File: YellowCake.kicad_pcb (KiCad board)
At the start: 2 copper layers, 95.9 x 90.2 mm, 4 parts

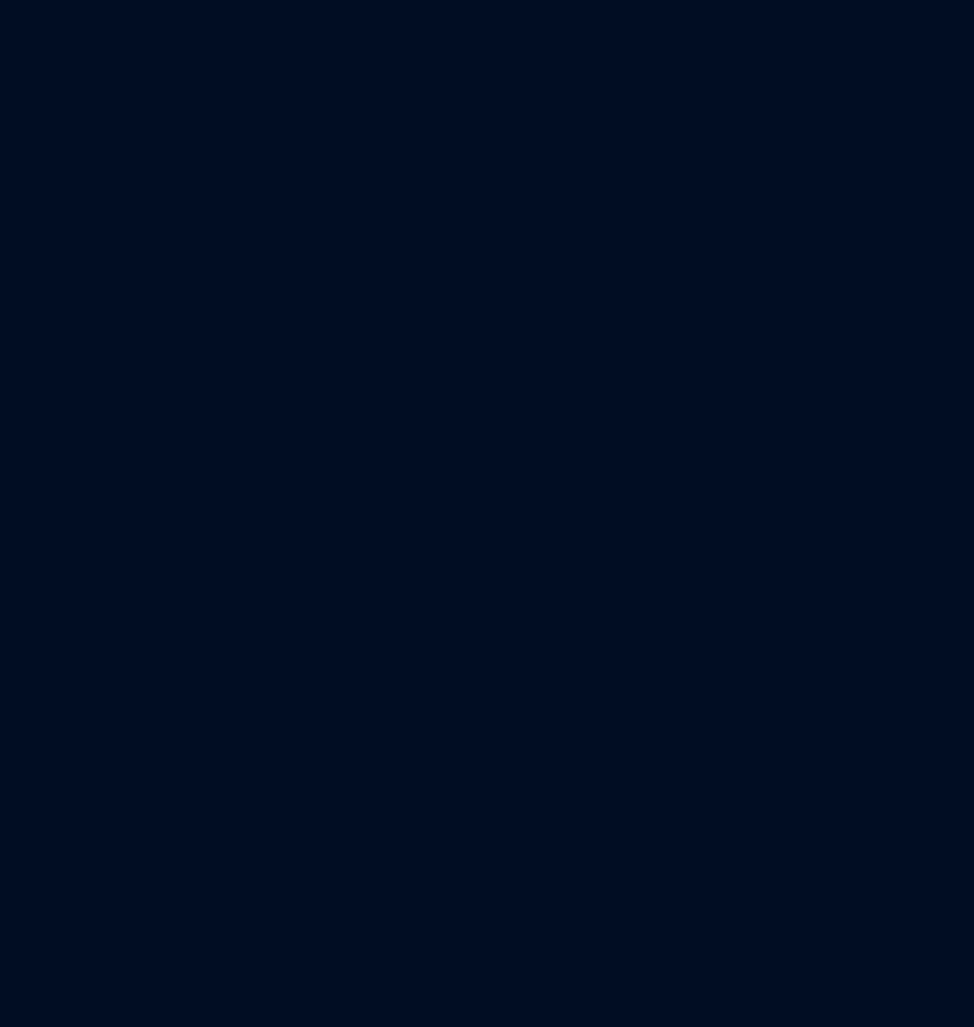
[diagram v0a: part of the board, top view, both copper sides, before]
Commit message: started power supply and DAC circuitry
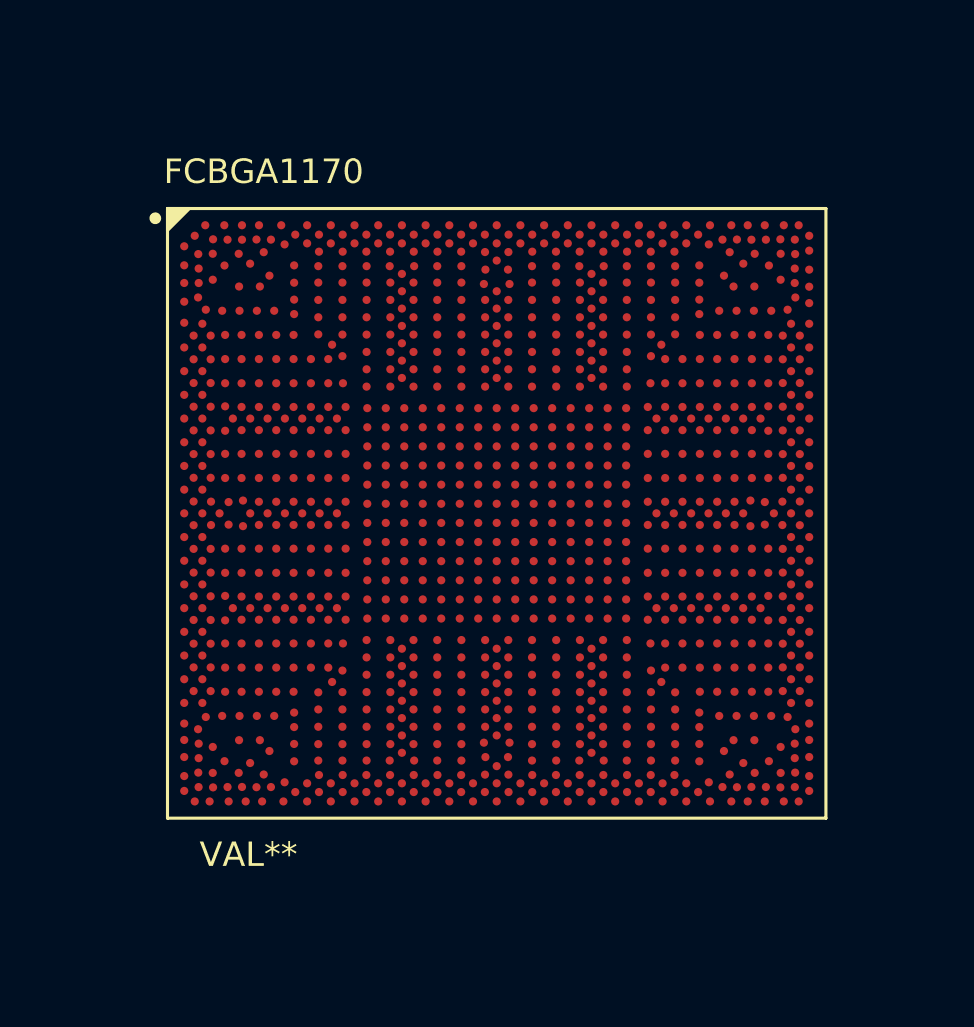
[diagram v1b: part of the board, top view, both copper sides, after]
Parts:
- added FCBGA1170: VAL**, Atom:FCBGA11702, F.Cu at (151.0, 83.0)

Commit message: finishing schematic
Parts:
- added C1, C11, C12, C14, C18, C21, C30, C34, C52, C53, C54, C55, C56, C57, C58, C61, C62, C66, C69, C71, C78, C79, C80, C81, C82, C83, C84, C85, C86, C9, C94, C95: 0.1uF, Capacitor_SMD:C_0603_1608Metric, F.Cu at (148.9, 138.3)
- added C10, C7: 10uF, Capacitor_Tantalum_SMD:CP_EIA-2012-15_AVX-P, F.Cu at (148.9, 138.3)
- added C100, C2, C3, C6, C96, C98: 1uF, Capacitor_SMD:C_0603_1608Metric, F.Cu at (148.9, 138.3)
- added C101: 4700PF, Capacitor_SMD:C_0603_1608Metric, F.Cu at (148.9, 138.3)
- added C102, C103, C13, C15, C76, C8, C89, C91, C97, C99: 10uF, Capacitor_SMD:C_0603_1608Metric, F.Cu at (148.9, 138.3)
- added C16, C17, C31, C33: 1000pF, Capacitor_SMD:C_0603_1608Metric, F.Cu at (148.9, 138.3)
- added C19, C22: 330pF, Capacitor_SMD:C_0603_1608Metric, F.Cu at (148.9, 138.3)
- added C20, C23: 0.01uF, Capacitor_SMD:C_0603_1608Metric, F.Cu at (148.9, 138.3)
- added C24, C28: 560pF, Capacitor_SMD:C_0603_1608Metric, F.Cu at (148.9, 138.3)
- added C25: 470pF, Capacitor_SMD:C_0603_1608Metric, F.Cu at (148.9, 138.3)
- added C26: 68pF, Capacitor_SMD:C_0603_1608Metric, F.Cu at (148.9, 138.3)
- added C27: 220pF, Capacitor_SMD:C_0603_1608Metric, F.Cu at (148.9, 138.3)
- added C29: 33pF, Capacitor_SMD:C_0603_1608Metric, F.Cu at (148.9, 138.3)
- added C32, C35, C37, C72, C77: 1.0uF, Capacitor_SMD:C_0603_1608Metric, F.Cu at (148.9, 138.3)
- added C36, C38, C39, C75: 0.22uF, Capacitor_SMD:C_0603_1608Metric, F.Cu at (148.9, 138.3)
- added C4, C5: 2.2uF, Capacitor_SMD:C_0603_1608Metric, F.Cu at (148.9, 138.3)
- added C40, C41: 2200pF, Capacitor_SMD:C_0603_1608Metric, F.Cu at (148.9, 138.3)
- added C42, C43: 0.047uF, Capacitor_SMD:C_0603_1608Metric, F.Cu at (148.9, 138.3)
- added C44, C45, C46, C47, C48, C49: 0.033uF, Capacitor_SMD:C_0603_1608Metric, F.Cu at (148.9, 138.3)
- added C59, C60, C67, C68, C70, C73, C74, C87, C88, C90, C92, C93: 22uF, Capacitor_SMD:C_0603_1608Metric, F.Cu at (148.9, 138.3)
- added C65: 8200pF, Resistor_SMD:R_0603_1608Metric, F.Cu at (148.9, 138.3)
- added D1, D4: BAT54A, Package_TO_SOT_SMD:SOT-23, F.Cu at (148.9, 138.3)
- added D2, D3: BAV99S, Package_TO_SOT_SMD:SOT-363_SC-70-6, F.Cu at (148.9, 138.3)
- added L1, L7, L8: 220Ohm, Inductor_SMD:L_0603_1608Metric, F.Cu at (148.9, 138.3)
- added L10, L4: 0Ohm, Inductor_SMD:L_0603_1608Metric, F.Cu at (148.9, 138.3)
- added L15: PIND-2.2U-8A, Inductor_SMD:L_0603_1608Metric, F.Cu at (148.9, 138.3)
- added Q1, Q2, Q4, Q5, Q6: 2N7002K, Package_TO_SOT_SMD:SOT-23, F.Cu at (148.9, 138.3)
- added Q3: MMBT3904, Package_TO_SOT_SMD:SOT-23, F.Cu at (148.9, 138.3)
- added R1, R2: 2.2kOhm, Resistor_SMD:R_0603_1608Metric, F.Cu at (148.9, 138.3)
- added R10, R32, R34, R36, R38, R39, R42, R43, R7, R8, R9: 0Ohm, Resistor_SMD:R_0603_1608Metric, F.Cu at (148.9, 138.3)
- added R100, R76, R77, R78, R79, R80, R81, R85, R87, R95, R97: 100KOhm, Resistor_SMD:R_0603_1608Metric, F.Cu at (148.9, 138.3)
- added R101: 200KOhm, Resistor_SMD:R_0603_1608Metric, F.Cu at (148.9, 138.3)
- added R11, R12, R14, R15: 10Ohm, Resistor_SMD:R_0603_1608Metric, F.Cu at (148.9, 138.3)
- added R13: 2.7KOhm, Resistor_SMD:R_0603_1608Metric, F.Cu at (148.9, 138.3)
- added R16: 2.32KOhm, Resistor_SMD:R_0603_1608Metric, F.Cu at (148.9, 138.3)
- added R17, R19: 200Ohm, Resistor_SMD:R_0603_1608Metric, F.Cu at (148.9, 138.3)
- added R18: 2.43KOhm, Resistor_SMD:R_0603_1608Metric, F.Cu at (148.9, 138.3)
- added R20, R23, R27: 80.6KOhm, Resistor_SMD:R_0603_1608Metric, F.Cu at (148.9, 138.3)
- added R21: 2.21KOhm, Resistor_SMD:R_0603_1608Metric, F.Cu at (148.9, 138.3)
- added R22, R24, R25: 69.8Ohm, Resistor_SMD:R_0603_1608Metric, F.Cu at (148.9, 138.3)
- added R26: 169KOhm, Resistor_SMD:R_0603_1608Metric, F.Cu at (148.9, 138.3)
- added R28, R30: 1.91KOhm, Resistor_SMD:R_0603_1608Metric, F.Cu at (148.9, 138.3)
- added R29, R31: 6.98KOhm, Resistor_SMD:R_0603_1608Metric, F.Cu at (148.9, 138.3)
- added R3, R4, R70, R71, R72, R73, R74, R75, R88: 33Ohm, Resistor_SMD:R_0603_1608Metric, F.Cu at (148.9, 138.3)
- added R33: 16.9Ohm, Resistor_SMD:R_0603_1608Metric, F.Cu at (148.9, 138.3)
- added R35: 20Ohm, Resistor_SMD:R_0603_1608Metric, F.Cu at (148.9, 138.3)
- added R37, R90, R91, R94: 1KOhm, Resistor_SMD:R_0603_1608Metric, F.Cu at (148.9, 138.3)
- added R40: 1Ohm, Resistor_SMD:R_0603_1608Metric, F.Cu at (148.9, 138.3)
- added R41, R48: 18.7KOhm, Resistor_SMD:R_0603_1608Metric, F.Cu at (148.9, 138.3)
- added R44, R47: 3.83KOhm, Resistor_SMD:R_0603_1608Metric, F.Cu at (148.9, 138.3)
- added R45, R46: NTC-470KOhm, Resistor_SMD:R_0603_1608Metric, F.Cu at (148.9, 138.3)
- added R49, R50: 649Ohm, Resistor_SMD:R_0603_1608Metric, F.Cu at (148.9, 138.3)
- added R5: 37.4KOhm, Resistor_SMD:R_0603_1608Metric, F.Cu at (148.9, 138.3)
- added R51: 2.67KOhm, Resistor_SMD:R_0603_1608Metric, F.Cu at (148.9, 138.3)
- added R52, R57: 2.61KOhm, Resistor_SMD:R_0603_1608Metric, F.Cu at (148.9, 138.3)
- added R53, R54: 11KOhm, Resistor_SMD:R_0603_1608Metric, F.Cu at (148.9, 138.3)
- added R55, R58: NTC-10KOhm, Resistor_SMD:R_0603_1608Metric, F.Cu at (148.9, 138.3)
- added R56: 2.55KOhm, Resistor_SMD:R_0603_1608Metric, F.Cu at (148.9, 138.3)
- added R6: 12.1KOhm, Resistor_SMD:R_0603_1608Metric, F.Cu at (148.9, 138.3)
- added R82, R84: 499KOhm, Resistor_SMD:R_0603_1608Metric, F.Cu at (148.9, 138.3)
- added R83: 2.2Ohms, Resistor_SMD:R_0603_1608Metric, F.Cu at (148.9, 138.3)
- added R86: 4.7Ohm, Resistor_SMD:R_0603_1608Metric, F.Cu at (148.9, 138.3)
- added R89: 2.2KOhm, Resistor_SMD:R_0603_1608Metric, F.Cu at (148.9, 138.3)
- added R92, R93: 10KOhm, Resistor_SMD:R_0603_1608Metric, F.Cu at (148.9, 138.3)
- added R99: 33KOhm, Resistor_SMD:R_0603_1608Metric, F.Cu at (148.9, 138.3)
- added U2: ISL95837HRZ-T, Package_DFN_QFN:QFN-40-1EP_6x6mm_P0.5mm_EP4.6x4.6mm, F.Cu at (148.9, 138.3)
- added U6: TPD4EUSB30, Package_SON:USON-10_2.5x1.0mm_P0.5mm, F.Cu at (148.9, 138.3)
- added U8: TPD6E001RSER, TPD6E001RSER:TPD6E001RSER, F.Cu at (148.9, 138.3)

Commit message: finished fixes
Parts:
- removed C1, C11, C12, C14, C18, C21, C30, C34, C52, C53, C54, C55, C56, C57, C58, C61, C62, C66, C69, C71, C78, C79, C80, C81, C82, C83, C84, C85, C86, C9, C94, C95: 0.1uF, Capacitor_SMD:C_0603_1608Metric
- removed C10, C7: 10uF, Capacitor_Tantalum_SMD:CP_EIA-2012-15_AVX-P
- removed C100, C2, C3, C6, C96, C98: 1uF, Capacitor_SMD:C_0603_1608Metric
- removed C101: 4700PF, Capacitor_SMD:C_0603_1608Metric
- removed C102, C103, C13, C15, C76, C8, C89, C91, C97, C99: 10uF, Capacitor_SMD:C_0603_1608Metric
- removed C16, C17, C31, C33: 1000pF, Capacitor_SMD:C_0603_1608Metric
- removed C19, C22: 330pF, Capacitor_SMD:C_0603_1608Metric
- removed C20, C23: 0.01uF, Capacitor_SMD:C_0603_1608Metric
- removed C24, C28: 560pF, Capacitor_SMD:C_0603_1608Metric
- removed C25: 470pF, Capacitor_SMD:C_0603_1608Metric
- removed C26: 68pF, Capacitor_SMD:C_0603_1608Metric
- removed C27: 220pF, Capacitor_SMD:C_0603_1608Metric
- removed C29: 33pF, Capacitor_SMD:C_0603_1608Metric
- removed C32, C35, C37, C72, C77: 1.0uF, Capacitor_SMD:C_0603_1608Metric
- removed C36, C38, C39, C75: 0.22uF, Capacitor_SMD:C_0603_1608Metric
- removed C4, C5: 2.2uF, Capacitor_SMD:C_0603_1608Metric
- removed C40, C41: 2200pF, Capacitor_SMD:C_0603_1608Metric
- removed C42, C43: 0.047uF, Capacitor_SMD:C_0603_1608Metric
- removed C44, C45, C46, C47, C48, C49: 0.033uF, Capacitor_SMD:C_0603_1608Metric
- removed C59, C60, C67, C68, C70, C73, C74, C87, C88, C90, C92, C93: 22uF, Capacitor_SMD:C_0603_1608Metric
- removed C65: 8200pF, Resistor_SMD:R_0603_1608Metric
- removed D1, D4: BAT54A, Package_TO_SOT_SMD:SOT-23
- removed D2, D3: BAV99S, Package_TO_SOT_SMD:SOT-363_SC-70-6
- removed L1, L7, L8: 220Ohm, Inductor_SMD:L_0603_1608Metric
- removed L10, L4: 0Ohm, Inductor_SMD:L_0603_1608Metric
- removed L15: PIND-2.2U-8A, Inductor_SMD:L_0603_1608Metric
- removed Q1, Q2, Q4, Q5, Q6: 2N7002K, Package_TO_SOT_SMD:SOT-23
- removed Q3: MMBT3904, Package_TO_SOT_SMD:SOT-23
- removed R1, R2: 2.2kOhm, Resistor_SMD:R_0603_1608Metric
- removed R10, R32, R34, R36, R38, R39, R42, R43, R7, R8, R9: 0Ohm, Resistor_SMD:R_0603_1608Metric
- removed R100, R76, R77, R78, R79, R80, R81, R85, R87, R95, R97: 100KOhm, Resistor_SMD:R_0603_1608Metric
- removed R101: 200KOhm, Resistor_SMD:R_0603_1608Metric
- removed R11, R12, R14, R15: 10Ohm, Resistor_SMD:R_0603_1608Metric
- removed R13: 2.7KOhm, Resistor_SMD:R_0603_1608Metric
- removed R16: 2.32KOhm, Resistor_SMD:R_0603_1608Metric
- removed R17, R19: 200Ohm, Resistor_SMD:R_0603_1608Metric
- removed R18: 2.43KOhm, Resistor_SMD:R_0603_1608Metric
- removed R20, R23, R27: 80.6KOhm, Resistor_SMD:R_0603_1608Metric
- removed R21: 2.21KOhm, Resistor_SMD:R_0603_1608Metric
- removed R22, R24, R25: 69.8Ohm, Resistor_SMD:R_0603_1608Metric
- removed R26: 169KOhm, Resistor_SMD:R_0603_1608Metric
- removed R28, R30: 1.91KOhm, Resistor_SMD:R_0603_1608Metric
- removed R29, R31: 6.98KOhm, Resistor_SMD:R_0603_1608Metric
- removed R3, R4, R70, R71, R72, R73, R74, R75, R88: 33Ohm, Resistor_SMD:R_0603_1608Metric
- removed R33: 16.9Ohm, Resistor_SMD:R_0603_1608Metric
- removed R35: 20Ohm, Resistor_SMD:R_0603_1608Metric
- removed R37, R90, R91, R94: 1KOhm, Resistor_SMD:R_0603_1608Metric
- removed R40: 1Ohm, Resistor_SMD:R_0603_1608Metric
- removed R41, R48: 18.7KOhm, Resistor_SMD:R_0603_1608Metric
- removed R44, R47: 3.83KOhm, Resistor_SMD:R_0603_1608Metric
- removed R45, R46: NTC-470KOhm, Resistor_SMD:R_0603_1608Metric
- removed R49, R50: 649Ohm, Resistor_SMD:R_0603_1608Metric
- removed R5: 37.4KOhm, Resistor_SMD:R_0603_1608Metric
- removed R51: 2.67KOhm, Resistor_SMD:R_0603_1608Metric
- removed R52, R57: 2.61KOhm, Resistor_SMD:R_0603_1608Metric
- removed R53, R54: 11KOhm, Resistor_SMD:R_0603_1608Metric
- removed R55, R58: NTC-10KOhm, Resistor_SMD:R_0603_1608Metric
- removed R56: 2.55KOhm, Resistor_SMD:R_0603_1608Metric
- removed R6: 12.1KOhm, Resistor_SMD:R_0603_1608Metric
- removed R82, R84: 499KOhm, Resistor_SMD:R_0603_1608Metric
- removed R83: 2.2Ohms, Resistor_SMD:R_0603_1608Metric
- removed R86: 4.7Ohm, Resistor_SMD:R_0603_1608Metric
- removed R89: 2.2KOhm, Resistor_SMD:R_0603_1608Metric
- removed R92, R93: 10KOhm, Resistor_SMD:R_0603_1608Metric
- removed R99: 33KOhm, Resistor_SMD:R_0603_1608Metric
- removed U2: ISL95837HRZ-T, Package_DFN_QFN:QFN-40-1EP_6x6mm_P0.5mm_EP4.6x4.6mm
- removed U6: TPD4EUSB30, Package_SON:USON-10_2.5x1.0mm_P0.5mm
- removed U8: TPD6E001RSER, TPD6E001RSER:TPD6E001RSER
- added TRANS_FDMD8530: VAL**, FDMS7602S:TRANS_FDMD8530, F.Cu at (174.6, 98.2)

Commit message: Finished all except RAM and CPU
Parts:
- removed REF** (x4): MountingHole_3.2mm_M3_Pad, MountingHole:MountingHole_3.2mm_M3_Pad
- removed TRANS_FDMD8530: VAL**, FDMS7602S:TRANS_FDMD8530
- added C1: 0.1uF, Capacitor_SMD:C_0603_1608Metric, F.Cu at (322.0, 119.4)
- added C10: 10uF, Capacitor_Tantalum_SMD:CP_EIA-2012-15_AVX-P, F.Cu at (318.5, 109.2)
- added C100: 1uF, Capacitor_SMD:C_0603_1608Metric, F.Cu at (152.4, 196.3)
- added C101: 4700PF, Capacitor_SMD:C_0603_1608Metric, F.Cu at (172.9, 180.9)
- added C102: 10uF, Capacitor_SMD:C_0603_1608Metric, F.Cu at (173.4, 175.9)
- added C103: 10uF, Capacitor_SMD:C_0603_1608Metric, F.Cu at (164.0, 188.9)
- added C104: 2.2uF, Capacitor_SMD:C_0603_1608Metric, F.Cu at (168.4, 183.0)
- added C105: 2.2uF, Capacitor_SMD:C_0603_1608Metric, F.Cu at (172.9, 178.4)
- added C106: 22pF, Capacitor_SMD:C_0603_1608Metric, F.Cu at (153.7, 198.9)
- added C107: 22pF, Capacitor_SMD:C_0603_1608Metric, F.Cu at (156.4, 195.6)
- added C108: 22pF, Capacitor_SMD:C_0603_1608Metric, F.Cu at (177.4, 173.4)
- added C109: 27pF, Capacitor_SMD:C_0603_1608Metric, F.Cu at (156.4, 193.1)
- added C11: 0.1uF, Capacitor_SMD:C_0603_1608Metric, F.Cu at (322.2, 114.3)
- added C110: 10uF, Capacitor_SMD:C_0603_1608Metric, F.Cu at (149.7, 198.9)
- added C111: 0.1uF, Capacitor_SMD:C_0603_1608Metric, F.Cu at (168.2, 186.3)
- added C112: 10uF, Capacitor_SMD:C_0603_1608Metric, F.Cu at (137.7, 200.1)
- added C113: 0.1uF, Capacitor_SMD:C_0603_1608Metric, F.Cu at (168.9, 180.5)
- added C114: 10uF, Capacitor_SMD:C_0603_1608Metric, F.Cu at (160.0, 189.9)
- added C115: 22pF, Capacitor_SMD:C_0603_1608Metric, F.Cu at (164.2, 186.3)
- added C116: 10uF, Capacitor_SMD:C_0603_1608Metric, F.Cu at (160.0, 187.4)
- added C117: 1.0uF, Capacitor_SMD:C_0603_1608Metric, F.Cu at (145.7, 199.8)
- added C118: 10uF, Capacitor_SMD:C_0603_1608Metric, F.Cu at (152.4, 193.8)
- added C119: 1uF, Capacitor_SMD:C_0603_1608Metric, F.Cu at (180.2, 185.9)
- added C12: 0.1uF, Capacitor_SMD:C_0603_1608Metric, F.Cu at (314.0, 117.8)
- added C120: 0.1uF, Capacitor_SMD:C_0603_1608Metric, F.Cu at (336.4, 183.8)
- added C121: 0.1uF, Capacitor_SMD:C_0603_1608Metric, F.Cu at (332.5, 188.8)
- added C122: 22uF, Capacitor_SMD:C_0603_1608Metric, F.Cu at (340.4, 180.7)
- added C123: 22uF, Capacitor_SMD:C_0603_1608Metric, F.Cu at (336.5, 186.3)
- added C124: 22uF, Capacitor_SMD:C_0603_1608Metric, F.Cu at (326.2, 176.5)
- added C125: 22uF, Capacitor_SMD:C_0603_1608Metric, F.Cu at (328.5, 186.6)
- added C126: 2200pF, Capacitor_SMD:C_0603_1608Metric, F.Cu at (316.4, 183.1)
- added C127: 2200pF, Capacitor_SMD:C_0603_1608Metric, F.Cu at (316.4, 185.6)
- added C128: 22uF, Capacitor_SMD:C_0603_1608Metric, F.Cu at (312.5, 188.9)
- added C129: 22uF, Capacitor_SMD:C_0603_1608Metric, F.Cu at (327.5, 173.7)
- added C13: 10uF, Capacitor_SMD:C_0603_1608Metric, F.Cu at (318.0, 120.3)
- added C130: 22uF, Capacitor_SMD:C_0603_1608Metric, F.Cu at (332.3, 170.7)
- added C131: 22uF, Capacitor_SMD:C_0603_1608Metric, F.Cu at (320.4, 183.1)
- added C132: 22uF, Capacitor_SMD:C_0603_1608Metric, F.Cu at (326.2, 179.0)
- added C133: 22uF, Capacitor_SMD:C_0603_1608Metric, F.Cu at (331.5, 173.7)
- added C134: 330uF, Capacitor_Tantalum_SMD:CP_EIA-7343-20_Kemet-V, F.Cu at (310.7, 178.2)
- added C135: 330uF, Capacitor_Tantalum_SMD:CP_EIA-7343-20_Kemet-V, F.Cu at (320.5, 172.3)
- added C136: 330uF, Capacitor_Tantalum_SMD:CP_EIA-7343-20_Kemet-V, F.Cu at (310.7, 172.3)
- added C137: 22uF, Capacitor_SMD:C_0603_1608Metric, F.Cu at (324.4, 183.1)
- added C138: 22uF, Capacitor_SMD:C_0603_1608Metric, F.Cu at (316.5, 190.6)
- added C139: 22uF, Capacitor_SMD:C_0603_1608Metric, F.Cu at (330.3, 178.7)
- added C14: 0.1uF, Capacitor_SMD:C_0603_1608Metric, F.Cu at (326.3, 111.5)
- added C140: 22uF, Capacitor_SMD:C_0603_1608Metric, F.Cu at (320.5, 188.1)
- added C141: 22uF, Capacitor_SMD:C_0603_1608Metric, F.Cu at (335.5, 173.2)
- added C142: 22uF, Capacitor_SMD:C_0603_1608Metric, F.Cu at (334.3, 176.2)
- added C143: 22uF, Capacitor_SMD:C_0603_1608Metric, F.Cu at (342.3, 178.2)
- added C144: 22uF, Capacitor_SMD:C_0603_1608Metric, F.Cu at (324.4, 185.6)
- added C145: 22uF, Capacitor_SMD:C_0603_1608Metric, F.Cu at (340.4, 183.2)
- added C146: 22uF, Capacitor_SMD:C_0603_1608Metric, F.Cu at (334.3, 178.7)
- added C147: 22uF, Capacitor_SMD:C_0603_1608Metric, F.Cu at (320.5, 190.6)
- added C148: 22uF, Capacitor_SMD:C_0603_1608Metric, F.Cu at (328.4, 181.5)
- added C149: 0.1uF, Capacitor_SMD:C_0603_1608Metric, F.Cu at (337.2, 136.0)
- added C15: 10uF, Capacitor_SMD:C_0603_1608Metric, F.Cu at (322.0, 116.9)
- added C150: 22uF, Capacitor_SMD:C_0603_1608Metric, F.Cu at (332.2, 141.3)
- added C151: 0.1uF, Capacitor_SMD:C_0603_1608Metric, F.Cu at (340.2, 146.1)
- added C152: 10uF, Capacitor_SMD:C_0603_1608Metric, F.Cu at (340.2, 143.6)
- added C153: 22uF, Capacitor_SMD:C_0603_1608Metric, F.Cu at (345.2, 138.6)
- added C154: 150pF, Capacitor_SMD:C_0603_1608Metric, F.Cu at (335.8, 148.8)
- added C155: 150pF, Capacitor_SMD:C_0603_1608Metric, F.Cu at (336.2, 146.1)
- added C156: 0.1uF, Capacitor_SMD:C_0603_1608Metric, F.Cu at (345.2, 136.0)
- added C157: 0.1uF, Capacitor_SMD:C_0603_1608Metric, F.Cu at (340.2, 141.1)
- added C158: 0.1uF, Capacitor_SMD:C_0603_1608Metric, F.Cu at (327.8, 148.9)
- added C159: 0.1uF, Capacitor_SMD:C_0603_1608Metric, F.Cu at (341.2, 138.6)
- added C16: 1000pF, Capacitor_SMD:C_0603_1608Metric, F.Cu at (239.5, 137.8)
- added C160: 10uF, Capacitor_SMD:C_0603_1608Metric, F.Cu at (331.8, 148.8)
- added C161: 10uF, Capacitor_SMD:C_0603_1608Metric, F.Cu at (328.2, 141.3)
- added C162: 10uF, Capacitor_SMD:C_0603_1608Metric, F.Cu at (333.1, 136.0)
- added C163: 0.1uF, Capacitor_SMD:C_0603_1608Metric, F.Cu at (344.2, 141.1)
- added C164: 22pF, Capacitor_SMD:C_0603_1608Metric, F.Cu at (333.1, 138.6)
- added C165: 10uF, Capacitor_SMD:C_0603_1608Metric, F.Cu at (328.2, 143.8)
- added C166: 0.1uF, Capacitor_SMD:C_0603_1608Metric, F.Cu at (224.5, 91.8)
- added C167: 1.0uF, Capacitor_SMD:C_0603_1608Metric, F.Cu at (238.5, 86.3)
- added C17: 1000pF, Capacitor_SMD:C_0603_1608Metric, F.Cu at (223.2, 152.9)
- added C18: 0.1uF, Capacitor_SMD:C_0603_1608Metric, F.Cu at (231.6, 145.3)
- added C19: 330pF, Capacitor_SMD:C_0603_1608Metric, F.Cu at (227.6, 147.8)
- added C2: 1uF, Capacitor_SMD:C_0603_1608Metric, F.Cu at (318.2, 111.8)
- added C20: 0.01uF, Capacitor_SMD:C_0603_1608Metric, F.Cu at (231.4, 140.3)
- added C21: 0.1uF, Capacitor_SMD:C_0603_1608Metric, F.Cu at (235.4, 140.3)
- added C22: 330pF, Capacitor_SMD:C_0603_1608Metric, F.Cu at (231.4, 142.8)
- added C23: 0.01uF, Capacitor_SMD:C_0603_1608Metric, F.Cu at (215.2, 158.6)
- added C24: 560pF, Capacitor_SMD:C_0603_1608Metric, F.Cu at (223.6, 150.3)
- added C25: 470pF, Capacitor_SMD:C_0603_1608Metric, F.Cu at (235.4, 137.8)
- added C26: 68pF, Capacitor_SMD:C_0603_1608Metric, F.Cu at (211.2, 160.6)
- added C27: 220pF, Capacitor_SMD:C_0603_1608Metric, F.Cu at (219.2, 152.9)
- added C28: 560pF, Capacitor_SMD:C_0603_1608Metric, F.Cu at (227.6, 145.3)
- added C29: 33pF, Capacitor_SMD:C_0603_1608Metric, F.Cu at (223.6, 147.8)
- added C3: 1uF, Capacitor_SMD:C_0603_1608Metric, F.Cu at (322.7, 109.0)
- added C30: 0.1uF, Capacitor_SMD:C_0603_1608Metric, F.Cu at (215.2, 156.1)
- added C31: 1000pF, Capacitor_SMD:C_0603_1608Metric, F.Cu at (223.4, 137.8)
- added C32: 1.0uF, Capacitor_SMD:C_0603_1608Metric, F.Cu at (211.2, 155.6)
- added C33: 1000pF, Capacitor_SMD:C_0603_1608Metric, F.Cu at (219.4, 137.8)
- added C34: 0.1uF, Capacitor_SMD:C_0603_1608Metric, F.Cu at (219.6, 145.3)
- added C35: 1.0uF, Capacitor_SMD:C_0603_1608Metric, F.Cu at (219.4, 142.8)
- added C36: 0.22uF, Capacitor_SMD:C_0603_1608Metric, F.Cu at (223.4, 140.3)
- added C37: 1.0uF, Capacitor_SMD:C_0603_1608Metric, F.Cu at (215.6, 148.6)
- added C38: 0.22uF, Capacitor_SMD:C_0603_1608Metric, F.Cu at (211.2, 153.1)
- added C39: 0.22uF, Capacitor_SMD:C_0603_1608Metric, F.Cu at (219.2, 157.9)
- added C4: 2.2uF, Capacitor_SMD:C_0603_1608Metric, F.Cu at (314.0, 120.3)
- added C40: 2200pF, Capacitor_SMD:C_0603_1608Metric, F.Cu at (227.6, 150.3)
- added C41: 2200pF, Capacitor_SMD:C_0603_1608Metric, F.Cu at (235.4, 142.8)
- added C42: 0.047uF, Capacitor_SMD:C_0603_1608Metric, F.Cu at (239.5, 140.3)
- added C43: 0.047uF, Capacitor_SMD:C_0603_1608Metric, F.Cu at (219.2, 160.4)
- added C44: 0.033uF, Capacitor_SMD:C_0603_1608Metric, F.Cu at (223.2, 155.4)
- added C45: 0.033uF, Capacitor_SMD:C_0603_1608Metric, F.Cu at (227.4, 137.8)
- added C46: 0.033uF, Capacitor_SMD:C_0603_1608Metric, F.Cu at (211.2, 150.6)
- added C47: 0.033uF, Capacitor_SMD:C_0603_1608Metric, F.Cu at (223.4, 142.8)
- added C48: 0.033uF, Capacitor_SMD:C_0603_1608Metric, F.Cu at (219.4, 140.3)
- added C49: 0.033uF, Capacitor_SMD:C_0603_1608Metric, F.Cu at (215.6, 146.0)
- added C5: 2.2uF, Capacitor_SMD:C_0603_1608Metric, F.Cu at (322.2, 111.8)
- added C50: 0.1uF, Capacitor_SMD:C_0603_1608Metric, F.Cu at (290.6, 132.5)
- added C51: 4.7uF, Capacitor_SMD:C_0603_1608Metric, F.Cu at (274.5, 130.3)
- added C52: 0.1uF, Capacitor_SMD:C_0603_1608Metric, F.Cu at (339.8, 34.9)
- added C53: 0.1uF, Capacitor_SMD:C_0603_1608Metric, F.Cu at (335.8, 39.9)
- added C54: 0.1uF, Capacitor_SMD:C_0603_1608Metric, F.Cu at (331.8, 39.9)
- added C55: 0.1uF, Capacitor_SMD:C_0603_1608Metric, F.Cu at (339.8, 37.4)
- added C56: 0.1uF, Capacitor_SMD:C_0603_1608Metric, F.Cu at (335.8, 37.4)
- added C57: 0.1uF, Capacitor_SMD:C_0603_1608Metric, F.Cu at (335.8, 34.9)
- added C58: 0.1uF, Capacitor_SMD:C_0603_1608Metric, F.Cu at (326.8, 38.0)
- added C59: 22uF, Capacitor_SMD:C_0603_1608Metric, F.Cu at (323.8, 40.5)
- added C6: 1uF, Capacitor_SMD:C_0603_1608Metric, F.Cu at (318.2, 114.3)
- added C60: 22uF, Capacitor_SMD:C_0603_1608Metric, F.Cu at (331.8, 36.4)
- added C61: 0.1uF, Capacitor_SMD:C_0603_1608Metric, F.Cu at (327.8, 40.5)
- added C62: 0.1uF, Capacitor_SMD:C_0603_1608Metric, F.Cu at (330.4, 33.9)
- added C63: 10uF, Capacitor_SMD:C_0603_1608Metric, F.Cu at (347.1, 78.4)
- added C64: 10uF, Capacitor_SMD:C_0603_1608Metric, F.Cu at (331.6, 93.4)
- added C65: 8200pF, Resistor_SMD:R_0603_1608Metric, F.Cu at (339.6, 83.4)
- added C66: 0.1uF, Capacitor_SMD:C_0603_1608Metric, F.Cu at (273.2, 188.1)
- added C67: 22uF, Capacitor_SMD:C_0603_1608Metric, F.Cu at (276.8, 193.1)
- added C68: 22uF, Capacitor_SMD:C_0603_1608Metric, F.Cu at (270.4, 199.6)
- added C69: 0.1uF, Capacitor_SMD:C_0603_1608Metric, F.Cu at (281.2, 188.1)
- added C7: 10uF, Capacitor_Tantalum_SMD:CP_EIA-2012-15_AVX-P, F.Cu at (309.7, 117.9)
- added C70: 22uF, Capacitor_SMD:C_0603_1608Metric, F.Cu at (264.0, 203.5)
- added C71: 0.1uF, Capacitor_SMD:C_0603_1608Metric, F.Cu at (277.0, 190.6)
- added C72: 1.0uF, Capacitor_SMD:C_0603_1608Metric, F.Cu at (256.0, 203.5)
- added C73: 22uF, Capacitor_SMD:C_0603_1608Metric, F.Cu at (277.2, 183.1)
- added C74: 22uF, Capacitor_SMD:C_0603_1608Metric, F.Cu at (269.0, 189.5)
- added C75: 0.22uF, Capacitor_SMD:C_0603_1608Metric, F.Cu at (273.2, 185.6)
- added C76: 10uF, Capacitor_SMD:C_0603_1608Metric, F.Cu at (258.4, 201.0)
- added C77: 1.0uF, Capacitor_SMD:C_0603_1608Metric, F.Cu at (252.0, 203.5)
- added C78: 0.1uF, Capacitor_SMD:C_0603_1608Metric, F.Cu at (262.4, 201.0)
- added C79: 0.1uF, Capacitor_SMD:C_0603_1608Metric, F.Cu at (276.0, 204.6)
- added C8: 10uF, Capacitor_SMD:C_0603_1608Metric, F.Cu at (318.0, 117.8)
- added C80: 0.1uF, Capacitor_SMD:C_0603_1608Metric, F.Cu at (281.0, 190.6)
- added C81: 0.1uF, Capacitor_SMD:C_0603_1608Metric, F.Cu at (278.5, 198.1)
- added C82: 0.1uF, Capacitor_SMD:C_0603_1608Metric, F.Cu at (280.8, 195.6)
- added C83: 0.1uF, Capacitor_SMD:C_0603_1608Metric, F.Cu at (272.0, 204.6)
- added C84: 0.1uF, Capacitor_SMD:C_0603_1608Metric, F.Cu at (272.0, 202.1)
- added C85: 0.1uF, Capacitor_SMD:C_0603_1608Metric, F.Cu at (285.0, 190.6)
- added C86: 0.1uF, Capacitor_SMD:C_0603_1608Metric, F.Cu at (280.8, 193.1)
- added C87: 22uF, Capacitor_SMD:C_0603_1608Metric, F.Cu at (274.5, 199.6)
- added C88: 22uF, Capacitor_SMD:C_0603_1608Metric, F.Cu at (268.0, 203.4)
- added C89: 10uF, Capacitor_SMD:C_0603_1608Metric, F.Cu at (266.4, 200.9)
- added C9: 0.1uF, Capacitor_SMD:C_0603_1608Metric, F.Cu at (326.7, 109.0)
- added C90: 22uF, Capacitor_SMD:C_0603_1608Metric, F.Cu at (276.8, 195.6)
- added C91: 10uF, Capacitor_SMD:C_0603_1608Metric, F.Cu at (264.8, 193.4)
- added C92: 22uF, Capacitor_SMD:C_0603_1608Metric, F.Cu at (285.2, 185.6)
- added C93: 22uF, Capacitor_SMD:C_0603_1608Metric, F.Cu at (276.0, 202.1)
- added C94: 0.1uF, Capacitor_SMD:C_0603_1608Metric, F.Cu at (263.7, 195.9)
- added C95: 0.1uF, Capacitor_SMD:C_0603_1608Metric, F.Cu at (284.8, 193.1)
- added C96: 1uF, Capacitor_SMD:C_0603_1608Metric, F.Cu at (176.4, 183.4)
- added C97: 10uF, Capacitor_SMD:C_0603_1608Metric, F.Cu at (176.9, 178.4)
- added C98: 1uF, Capacitor_SMD:C_0603_1608Metric, F.Cu at (173.4, 173.4)
- added C99: 10uF, Capacitor_SMD:C_0603_1608Metric, F.Cu at (168.9, 177.9)
- added D1: BAT54A, Package_TO_SOT_SMD:SOT-23, F.Cu at (211.4, 147.1)
- added D2: BAV99S, Package_TO_SOT_SMD:SOT-363_SC-70-6, F.Cu at (247.8, 204.1)
- added D3: BAV99S, Package_TO_SOT_SMD:SOT-363_SC-70-6, F.Cu at (264.9, 190.2)
- added D4: BAT54A, Package_TO_SOT_SMD:SOT-23, F.Cu at (151.5, 190.3)
- added D5: APTR3216-VFX, LED_SMD:LED_1206_3216Metric, F.Cu at (146.4, 189.7)
- added D6: APTR3216-VFX, LED_SMD:LED_1206_3216Metric, F.Cu at (154.9, 181.8)
- added D7: D5V0L1B2LP-7B, Diode_SMD:D_01005_0402Metric, F.Cu at (132.5, 200.4)
- added D8: BAT54A, Package_TO_SOT_SMD:SOT-23, F.Cu at (164.7, 174.4)
- added D9: BAT54C, Package_TO_SOT_SMD:SOT-23, F.Cu at (238.7, 82.8)
- added F1: 2A, Fuse:Fuse_0603_1608Metric, F.Cu at (347.8, 37.4)
- added H1: MountingHole_Pad, MountingHole:MountingHole_3.2mm_M3_Pad, F.Cu at (152.6, 176.1)
- added H2: MountingHole_Pad, MountingHole:MountingHole_3.2mm_M3_Pad, F.Cu at (143.5, 184.1)
- added H3: MountingHole_Pad, MountingHole:MountingHole_3.2mm_M3_Pad, F.Cu at (135.1, 189.6)
- added H4: MountingHole_Pad, MountingHole:MountingHole_3.2mm_M3_Pad, F.Cu at (144.6, 176.1)
- added J1: 10029449-111RLF, 10029449-111RLF:10029449-111RLF, F.Cu at (273.4, 118.3)
- added J2: USB_A, Connector_USB:USB_A_CNCTech_1001-011-01101_Horizontal, F.Cu at (324.1, 25.0)
- added J3: USB3_A, Connector_USB:USB3_A_Molex_48393-001, F.Cu at (340.6, 20.8)
- added J4: SODIMM-200, 2013289-1:2013289-1, F.Cu at (149.2, 53.8)
- added J5: Micro_SD_Card, Connector_Card:microSD_HC_Hirose_DM3AT-SF-PEJM5, F.Cu at (321.2, 86.4)
- added J6: Conn_Coaxial_Power, Connector_BarrelJack:BarrelJack_Horizontal, F.Cu at (260.2, 187.2)
- added J7: Conn_01x08_Male, Connector_PinHeader_1.00mm:PinHeader_1x08_P1.00mm_Vertical_SMD_Pin1Left, F.Cu at (225.3, 85.5)
- added JP1: Jumper, Jumper:SolderJumper-2_P1.3mm_Open_RoundedPad1.0x1.5mm, F.Cu at (148.2, 194.4)
- added L1: 220Ohm, Inductor_SMD:L_0603_1608Metric, F.Cu at (326.3, 114.0)
- added L10: 0Ohm, Inductor_SMD:L_0603_1608Metric, F.Cu at (351.8, 34.9)
- added L11: FB_120R_3A, Inductor_SMD:L_0603_1608Metric, F.Cu at (273.2, 183.1)
- added L12: FB_120R_3A, Inductor_SMD:L_0603_1608Metric, F.Cu at (263.7, 198.4)
- added L13: FB_120R_3A, Inductor_SMD:L_0603_1608Metric, F.Cu at (277.2, 185.6)
- added L14: FB_120R_3A, Inductor_SMD:L_0603_1608Metric, F.Cu at (281.2, 183.1)
- added L15: PIND-2.2U-8A, Inductor_SMD:L_0603_1608Metric, F.Cu at (273.0, 190.6)
- added L16: INDUCTOR, Inductor_SMD:L_0603_1608Metric, F.Cu at (141.7, 200.1)
- added L17: FB_120R_3A, Inductor_SMD:L_0603_1608Metric, F.Cu at (336.3, 170.7)
- added L18: FB_120R_3A, Inductor_SMD:L_0603_1608Metric, F.Cu at (316.5, 188.1)
- added L19: ACM2012-900-2P-T, ACM2012-900-2P-T:ACM2012-900-2P-T, F.Cu at (328.0, 170.9)
- added L2: FB_220R_2.2A, Inductor_SMD:L_0603_1608Metric, F.Cu at (270.5, 130.3)
- added L20: ACM2012-900-2P-T, ACM2012-900-2P-T:ACM2012-900-2P-T, F.Cu at (308.2, 189.2)
- added L21: 0.33uH, Inductor_SMD:L_0603_1608Metric, F.Cu at (320.4, 185.6)
- added L22: 0.33uH, Inductor_SMD:L_0603_1608Metric, F.Cu at (330.3, 176.2)
- added L3: ACM2012-900, ACM2012-900-2P-T:ACM2012-900-2P-T, F.Cu at (323.3, 35.2)
- added L4: 0Ohm, Inductor_SMD:L_0603_1608Metric, F.Cu at (354.1, 29.1)
- added L5: ACM2012-900, ACM2012-900-2P-T:ACM2012-900-2P-T, F.Cu at (314.7, 40.8)
- added L6: ACM2012-900, ACM2012-900-2P-T:ACM2012-900-2P-T, F.Cu at (354.6, 18.8)
- added L7: 220Ohm, Inductor_SMD:L_0603_1608Metric, F.Cu at (343.8, 39.9)
- added L8: 220Ohm, Inductor_SMD:L_0603_1608Metric, F.Cu at (354.1, 26.6)
- added L9: ACM2012-900, ACM2012-900-2P-T:ACM2012-900-2P-T, F.Cu at (319.5, 40.8)
- added Q1: 2N7002K, Package_TO_SOT_SMD:SOT-23, F.Cu at (159.9, 183.8)
- added Q2: 2N7002K, Package_TO_SOT_SMD:SOT-23, F.Cu at (169.1, 174.4)
- added Q3: MMBT3904, Package_TO_SOT_SMD:SOT-23, F.Cu at (164.7, 179.0)
- added Q4: 2N7002K, Package_TO_SOT_SMD:SOT-23, F.Cu at (143.8, 196.3)
- added Q5: 2N7002K, Package_TO_SOT_SMD:SOT-23, F.Cu at (154.3, 185.8)
- added Q6: 2N7002K, Package_TO_SOT_SMD:SOT-23, F.Cu at (159.9, 179.3)
- added Q7: MBT3904DW1, Package_TO_SOT_SMD:SOT-363_SC-70-6, F.Cu at (164.3, 183.2)
- added Q8: MBT3904DW1, Package_TO_SOT_SMD:SOT-363_SC-70-6, F.Cu at (155.8, 190.0)
- added Q9: BSS138, Package_TO_SOT_SMD:SOT-23, F.Cu at (243.2, 82.8)
- added R1: 2.2kOhm, Resistor_SMD:R_0603_1608Metric, F.Cu at (326.0, 116.9)
- added R10: 0Ohm, Resistor_SMD:R_0603_1608Metric, F.Cu at (243.7, 150.3)
- added R100: 100KOhm, Resistor_SMD:R_0603_1608Metric, F.Cu at (181.0, 178.4)
- added R101: 200KOhm, Resistor_SMD:R_0603_1608Metric, F.Cu at (168.4, 193.9)
- added R102: RQ5E035ATTCL, RQ5E035ATTCL:RQ5E035ATTCL, F.Cu at (133.4, 196.3)
- added R103: RQ5E035ATTCL, RQ5E035ATTCL:RQ5E035ATTCL, F.Cu at (141.3, 190.7)
- added R104: 2.2KOhm, Resistor_SMD:R_0603_1608Metric, F.Cu at (343.8, 34.9)
- added R105: 2.2KOhm, Resistor_SMD:R_0603_1608Metric, F.Cu at (354.1, 24.1)
- added R106: 10KOhm, Resistor_SMD:R_0603_1608Metric, F.Cu at (322.7, 38.0)
- added R107: 10KOhm, Resistor_SMD:R_0603_1608Metric, F.Cu at (347.8, 34.9)
- added R108: 10KOhm, Resistor_SMD:R_0603_1608Metric, F.Cu at (339.8, 39.9)
- added R109: 2.2KOhm, Resistor_SMD:R_0603_1608Metric, F.Cu at (343.8, 37.4)
- added R11: 10Ohm, Resistor_SMD:R_0603_1608Metric, F.Cu at (235.2, 152.9)
- added R110: 2.2KOhm, Resistor_SMD:R_0603_1608Metric, F.Cu at (354.1, 21.6)
- added R111: 1Ohm, Resistor_SMD:R_0603_1608Metric, F.Cu at (165.7, 196.4)
- added R112: 148Ohm, Resistor_SMD:R_0603_1608Metric, F.Cu at (172.4, 191.4)
- added R113: 146Ohm, Resistor_SMD:R_0603_1608Metric, F.Cu at (180.4, 183.4)
- added R114: 40.2KOhm, Resistor_SMD:R_0603_1608Metric, F.Cu at (176.0, 188.5)
- added R115: 40.2KOhm, Resistor_SMD:R_0603_1608Metric, F.Cu at (165.7, 198.9)
- added R116: 1kOhm, Resistor_SMD:R_0603_1608Metric, F.Cu at (181.0, 180.9)
- added R117: 10kOhm, Resistor_SMD:R_0603_1608Metric, F.Cu at (169.7, 196.4)
- added R118: 4.7kOhm, Resistor_SMD:R_0603_1608Metric, F.Cu at (160.4, 192.4)
- added R119: RQ5E035ATTCL, RQ5E035ATTCL:RQ5E035ATTCL, F.Cu at (149.8, 182.8)
- added R12: 10Ohm, Resistor_SMD:R_0603_1608Metric, F.Cu at (239.2, 152.9)
- added R120: 4.7kOhm, Resistor_SMD:R_0603_1608Metric, F.Cu at (160.4, 194.9)
- added R121: 4.7kOhm, Resistor_SMD:R_0603_1608Metric, F.Cu at (157.7, 198.2)
- added R122: 0Ohm, Resistor_SMD:R_0603_1608Metric, F.Cu at (172.4, 183.4)
- added R123: 10kOhm, Resistor_SMD:R_0603_1608Metric, F.Cu at (168.0, 188.9)
- added R124: 10Ohm, Resistor_SMD:R_0603_1608Metric, F.Cu at (176.9, 180.9)
- added R125: 200kOhm, Resistor_SMD:R_0603_1608Metric, F.Cu at (164.4, 193.9)
- added R126: 20kOhm, Resistor_SMD:R_0603_1608Metric, F.Cu at (172.2, 185.9)
- added R127: 20kOhm, Resistor_SMD:R_0603_1608Metric, F.Cu at (164.4, 191.4)
- added R128: 0Ohm, Resistor_SMD:R_0603_1608Metric, F.Cu at (339.5, 173.2)
- added R129: 0Ohm, Resistor_SMD:R_0603_1608Metric, F.Cu at (324.5, 188.1)
- added R13: 2.7KOhm, Resistor_SMD:R_0603_1608Metric, F.Cu at (247.7, 145.3)
- added R130: 0Ohm, Resistor_SMD:R_0603_1608Metric, F.Cu at (338.3, 175.7)
- added R131: 0Ohm, Resistor_SMD:R_0603_1608Metric, F.Cu at (332.4, 181.3)
- added R132: 10KOhm, Resistor_SMD:R_0603_1608Metric, F.Cu at (324.5, 190.6)
- added R133: 10KOhm, Resistor_SMD:R_0603_1608Metric, F.Cu at (338.3, 178.2)
- added R134: 2.2Ohm, Resistor_SMD:R_0603_1608Metric, F.Cu at (332.4, 183.8)
- added R135: 1KOhm, Resistor_SMD:R_0603_1608Metric, F.Cu at (340.3, 170.7)
- added R136: 1Ohm, Resistor_SMD:R_0603_1608Metric, F.Cu at (343.5, 173.2)
- added R137: 2.2Ohm, Resistor_SMD:R_0603_1608Metric, F.Cu at (342.3, 175.7)
- added R138: 1KOhm, Resistor_SMD:R_0603_1608Metric, F.Cu at (328.5, 189.1)
- added R139: 1Ohm, Resistor_SMD:R_0603_1608Metric, F.Cu at (336.4, 181.3)
- added R14: 10Ohm, Resistor_SMD:R_0603_1608Metric, F.Cu at (243.7, 147.8)
- added R140: 0Ohm, Resistor_SMD:R_0603_1608Metric, F.Cu at (332.5, 186.3)
- added R141: 0Ohm, Resistor_SMD:R_0603_1608Metric, F.Cu at (328.4, 184.1)
- added R142: 6.04KOhm, Resistor_SMD:R_0603_1608Metric, F.Cu at (328.2, 146.3)
- added R143: 23.7KOhm, Resistor_SMD:R_0603_1608Metric, F.Cu at (319.7, 148.9)
- added R144: 12.1KOhm, Resistor_SMD:R_0603_1608Metric, F.Cu at (337.2, 138.6)
- added R145: 9.53KOhm, Resistor_SMD:R_0603_1608Metric, F.Cu at (332.2, 143.8)
- added R146: 10KOhm, Resistor_SMD:R_0603_1608Metric, F.Cu at (336.2, 141.1)
- added R147: 4.7KOhm, Resistor_SMD:R_0603_1608Metric, F.Cu at (341.2, 136.0)
- added R148: 4.7KOhm, Resistor_SMD:R_0603_1608Metric, F.Cu at (332.2, 146.3)
- added R149: 4.7KOhm, Resistor_SMD:R_0603_1608Metric, F.Cu at (323.7, 148.9)
- added R15: 10Ohm, Resistor_SMD:R_0603_1608Metric, F.Cu at (235.2, 155.4)
- added R150: 0Ohm, Resistor_SMD:R_0603_1608Metric, F.Cu at (336.2, 143.6)
- added R151: 4.7KOhm, Resistor_SMD:R_0603_1608Metric, F.Cu at (344.2, 143.6)
- added R152: 0Ohm, Resistor_SMD:R_0603_1608Metric, F.Cu at (344.2, 146.1)
- added R153: 12.1KOhm, Resistor_SMD:R_0603_1608Metric, F.Cu at (343.8, 148.6)
- added R154: 12.1KOhm, Resistor_SMD:R_0603_1608Metric, F.Cu at (339.8, 148.6)
- added R155: 10KOhm, Resistor_SMD:R_0603_1608Metric, F.Cu at (242.5, 86.3)
- added R156: 10KOhm, Resistor_SMD:R_0603_1608Metric, F.Cu at (236.5, 88.8)
- added R157: 10KOhm, Resistor_SMD:R_0603_1608Metric, F.Cu at (236.5, 91.3)
- added R158: 10KOhm, Resistor_SMD:R_0603_1608Metric, F.Cu at (240.5, 88.8)
- added R16: 2.32KOhm, Resistor_SMD:R_0603_1608Metric, F.Cu at (231.2, 160.4)
- added R17: 200Ohm, Resistor_SMD:R_0603_1608Metric, F.Cu at (251.5, 140.3)
- added R18: 2.43KOhm, Resistor_SMD:R_0603_1608Metric, F.Cu at (243.2, 152.9)
- added R19: 200Ohm, Resistor_SMD:R_0603_1608Metric, F.Cu at (239.7, 150.3)
- added R2: 2.2kOhm, Resistor_SMD:R_0603_1608Metric, F.Cu at (326.0, 119.4)
- added R20: 80.6KOhm, Resistor_SMD:R_0603_1608Metric, F.Cu at (231.2, 157.9)
- added R21: 2.21KOhm, Resistor_SMD:R_0603_1608Metric, F.Cu at (251.5, 137.8)
- added R22: 69.8Ohm, Resistor_SMD:R_0603_1608Metric, F.Cu at (219.2, 155.4)
- added R23: 80.6KOhm, Resistor_SMD:R_0603_1608Metric, F.Cu at (227.4, 142.8)
- added R24: 69.8Ohm, Resistor_SMD:R_0603_1608Metric, F.Cu at (219.6, 150.3)
- added R25: 69.8Ohm, Resistor_SMD:R_0603_1608Metric, F.Cu at (211.2, 158.1)
- added R26: 169KOhm, Resistor_SMD:R_0603_1608Metric, F.Cu at (231.4, 137.8)
- added R27: 80.6KOhm, Resistor_SMD:R_0603_1608Metric, F.Cu at (215.2, 153.6)
- added R28: 1.91KOhm, Resistor_SMD:R_0603_1608Metric, F.Cu at (223.6, 145.3)
- added R29: 6.98KOhm, Resistor_SMD:R_0603_1608Metric, F.Cu at (219.6, 147.8)
- added R3: 33Ohm, Resistor_SMD:R_0603_1608Metric, F.Cu at (330.0, 116.6)
- added R30: 1.91KOhm, Resistor_SMD:R_0603_1608Metric, F.Cu at (227.4, 140.3)
- added R31: 6.98KOhm, Resistor_SMD:R_0603_1608Metric, F.Cu at (215.2, 151.1)
- added R32: 0Ohm, Resistor_SMD:R_0603_1608Metric, F.Cu at (247.5, 142.8)
- added R33: 16.9Ohm, Resistor_SMD:R_0603_1608Metric, F.Cu at (231.2, 155.4)
- added R34: 0Ohm, Resistor_SMD:R_0603_1608Metric, F.Cu at (231.6, 147.8)
- added R35: 20Ohm, Resistor_SMD:R_0603_1608Metric, F.Cu at (231.2, 152.9)
- added R36: 0Ohm, Resistor_SMD:R_0603_1608Metric, F.Cu at (247.5, 137.8)
- added R37: 1KOhm, Resistor_SMD:R_0603_1608Metric, F.Cu at (227.2, 157.9)
- added R38: 0Ohm, Resistor_SMD:R_0603_1608Metric, F.Cu at (235.7, 150.3)
- added R39: 0Ohm, Resistor_SMD:R_0603_1608Metric, F.Cu at (243.5, 142.8)
- added R4: 33Ohm, Resistor_SMD:R_0603_1608Metric, F.Cu at (330.0, 119.1)
- added R40: 1Ohm, Resistor_SMD:R_0603_1608Metric, F.Cu at (247.5, 140.3)
- added R41: 18.7KOhm, Resistor_SMD:R_0603_1608Metric, F.Cu at (227.2, 160.4)
- added R42: 0Ohm, Resistor_SMD:R_0603_1608Metric, F.Cu at (239.7, 147.8)
- added R43: 0Ohm, Resistor_SMD:R_0603_1608Metric, F.Cu at (243.7, 145.3)
- added R44: 3.83KOhm, Resistor_SMD:R_0603_1608Metric, F.Cu at (235.2, 157.9)
- added R45: NTC-470KOhm, Resistor_SMD:R_0603_1608Metric, F.Cu at (227.2, 155.4)
- added R46: NTC-470KOhm, Resistor_SMD:R_0603_1608Metric, F.Cu at (223.2, 160.4)
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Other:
- outline, holes or cut-outs redrawn

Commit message: fixed fanout
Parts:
- C50, J5, R59, R60, R61, R62, R65, R66, R67, R68, U8: moved to B.Cu
- moved C63 316.2 mm to (34.8, 28.7)
- moved R75 315.8 mm to (31.3, 28.0), turned to 90 degrees
- moved C65 313.7 mm to (29.6, 35.4), turned to 180 degrees
- moved R71 309.7 mm to (38.0, 27.9), turned to 90 degrees
- moved R80 309.6 mm to (33.2, 30.3), turned to 180 degrees
- moved R81 306.6 mm to (32.1, 33.7), turned to 180 degrees
- moved R73 304.7 mm to (34.6, 38.4), turned to 90 degrees
- moved R76 304.3 mm to (38.2, 35.4)
- moved R78 303.7 mm to (36.0, 33.7)
- moved R74 303.3 mm to (32.4, 38.4), turned to 90 degrees
- moved C64 302.3 mm to (34.9, 35.4), turned to 180 degrees
- moved R72 300.9 mm to (36.8, 38.4), turned to 90 degrees
- moved R79 300.6 mm to (35.4, 32.0), turned to 180 degrees
- moved R77 299.6 mm to (37.2, 30.3)
- moved C52 299.2 mm to (60.0, 140.9)
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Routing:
- net (no net): track 0.00 -> 76.0 mm, vias 0 -> 140
- net Net-(J1-Pad16): track 0.00 -> 33.1 mm, vias 0 -> 4
- net Net-(J1-Pad15): track 0.00 -> 30.1 mm, vias 0 -> 2
- net +V1P8S: track 0.00 -> 27.7 mm, vias 0 -> 1
- net +3V3: track 0.00 -> 24.2 mm, vias 0 -> 1
- net Net-(J5-Pad8): track 0.00 -> 23.2 mm, vias 0 -> 1
- net Net-(J1-Pad19): track 0.00 -> 22.8 mm, vias 0 -> 2
- net Net-(J1-Pad13): track 0.00 -> 19.4 mm, vias 0 -> 2
- net HDMI_TX1_DN: track 0.00 -> 18.8 mm
- net HDMI_TX1_DP: track 0.00 -> 18.8 mm
- net HDMI_CLK_DP: track 0.00 -> 18.8 mm
- net HDMI_TX0_DP: track 0.00 -> 18.7 mm
- net HDMI_CLK_DN: track 0.00 -> 18.7 mm
- net HDMI_TX0_DN: track 0.00 -> 18.6 mm
- net HDMI_TX2_DN: track 0.00 -> 18.1 mm, vias 0 -> 2
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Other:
- copper layers 2 -> 4
- net class Default: clearance 0.2 -> 0.05
- rule pad_to_mask_clearance: 0.051 -> 0
- rule trace_clearance: 0.2 -> 0.05
- rule trace_min: 0.2 -> 0.09
- rule via_min_drill: 0.3 -> 0.2
